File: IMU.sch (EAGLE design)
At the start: 3 parts

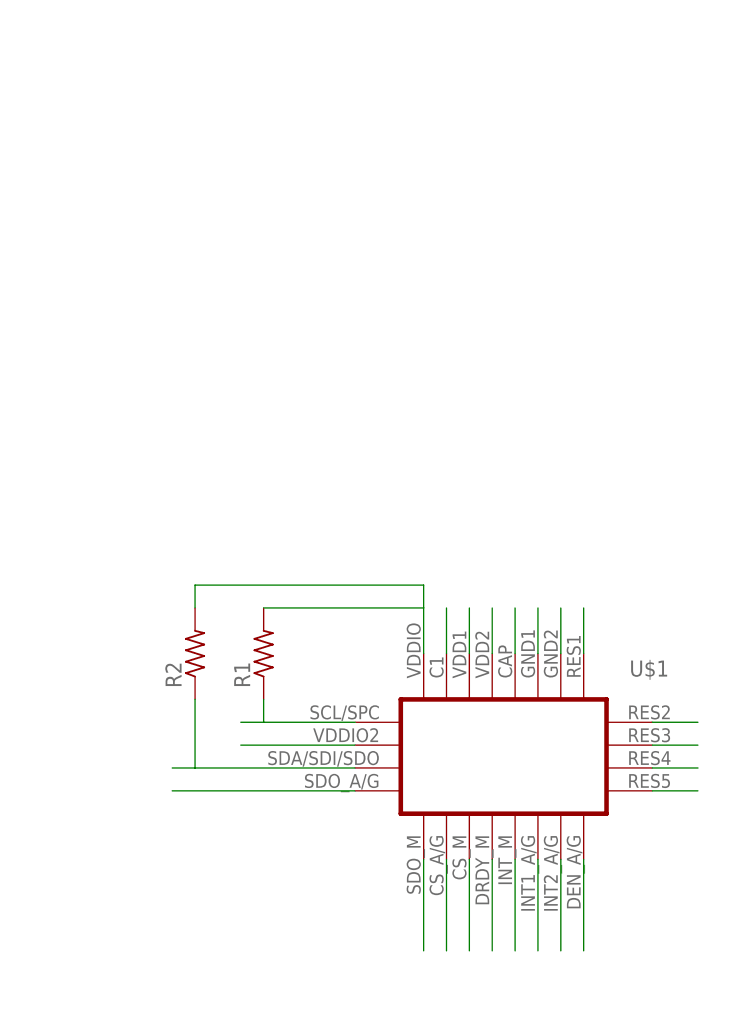
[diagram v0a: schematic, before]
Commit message: added IMU to quadcopter
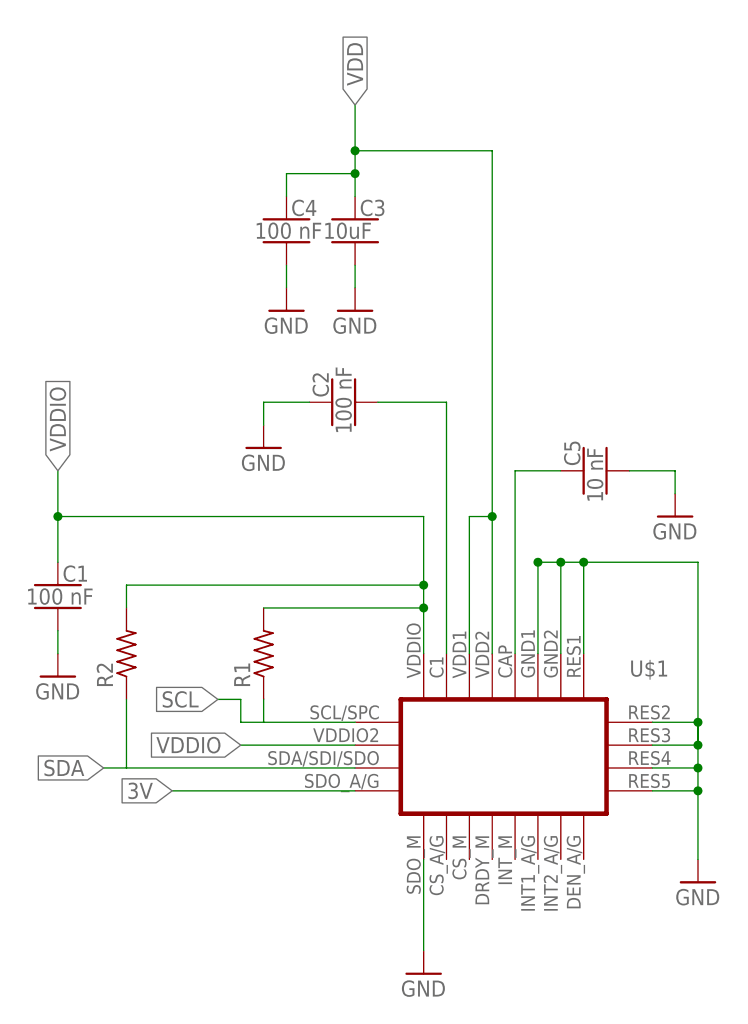
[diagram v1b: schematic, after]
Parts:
- added C1, C2, C4: 100 nF, quadparts_prebuilt:CAPACITOR-NP_SMD-2012-0805_CERAMIC
- added C3: 10uF, quadparts_prebuilt:CAPACITOR-NP_SMD-2012-0805_CERAMIC-10UF
- added C5: 10 nF, quadparts_prebuilt:CAPACITOR-NP_SMD-2012-0805_CERAMIC
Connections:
- net N$1 renamed 3V
- net N$24 renamed SCL
- net N$4 renamed SDA
- removed net N$10: U$1.INT1_A/G
- removed net N$11: U$1.INT2_A/G
- removed net N$12: U$1.DEN_A/G
- removed net N$13: U$1.RES5
- removed net N$14: U$1.RES4
- removed net N$15: U$1.RES3
- removed net N$16: U$1.RES2
- removed net N$17: U$1.RES1
- removed net N$18: U$1.GND2
- removed net N$19: U$1.GND1
- removed net N$2: U$1.VDDIO2
- removed net N$21: U$1.VDD2
- removed net N$22: U$1.VDD1
- removed net N$3: R1.2, R2.2, U$1.VDDIO1
- removed net N$5: U$1.SDO_M
- removed net N$6: U$1.CS_A/G
- removed net N$7: U$1.CS_M
- removed net N$8: U$1.DRDY_M
- removed net N$9: U$1.INT_M
- new net GND: C1.2, C2.1, C3.2, C4.2, C5.2, U$1.GND1, U$1.GND2, U$1.RES1, U$1.RES2, U$1.RES3, U$1.RES4, U$1.RES5, U$1.SDO_M
- new net VDD: C3.1, C4.1, U$1.VDD1, U$1.VDD2
- new net VDDIO: C1.1, R1.2, R2.2, U$1.VDDIO1, U$1.VDDIO2
- net N$20: now also C5.1
- net N$23: now also C2.2
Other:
- moved on the sheet: R2
